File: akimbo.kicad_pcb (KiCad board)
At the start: 2 copper layers, 163.9 x 125.9 mm, 77 parts, among them J1 USB-C, J2 3.5mm TRRS, J3 3.5mm TRRS, K1 -, K11 -, K12 -, K13 -, K14 -, K15 -, K16 -, K17 -, K18 -, K19 -, K2 -, K20 -, K21 -, K22 -, K23 -, K24 -, K25 -, K26 -, K27 -, K28 -, K29 -, K3 -, K30 -, K4 -, K6 -, K7 -, K8 -, K9 -, U1 ATmega32U4, U2 MCP23017_SO, Y1 16M

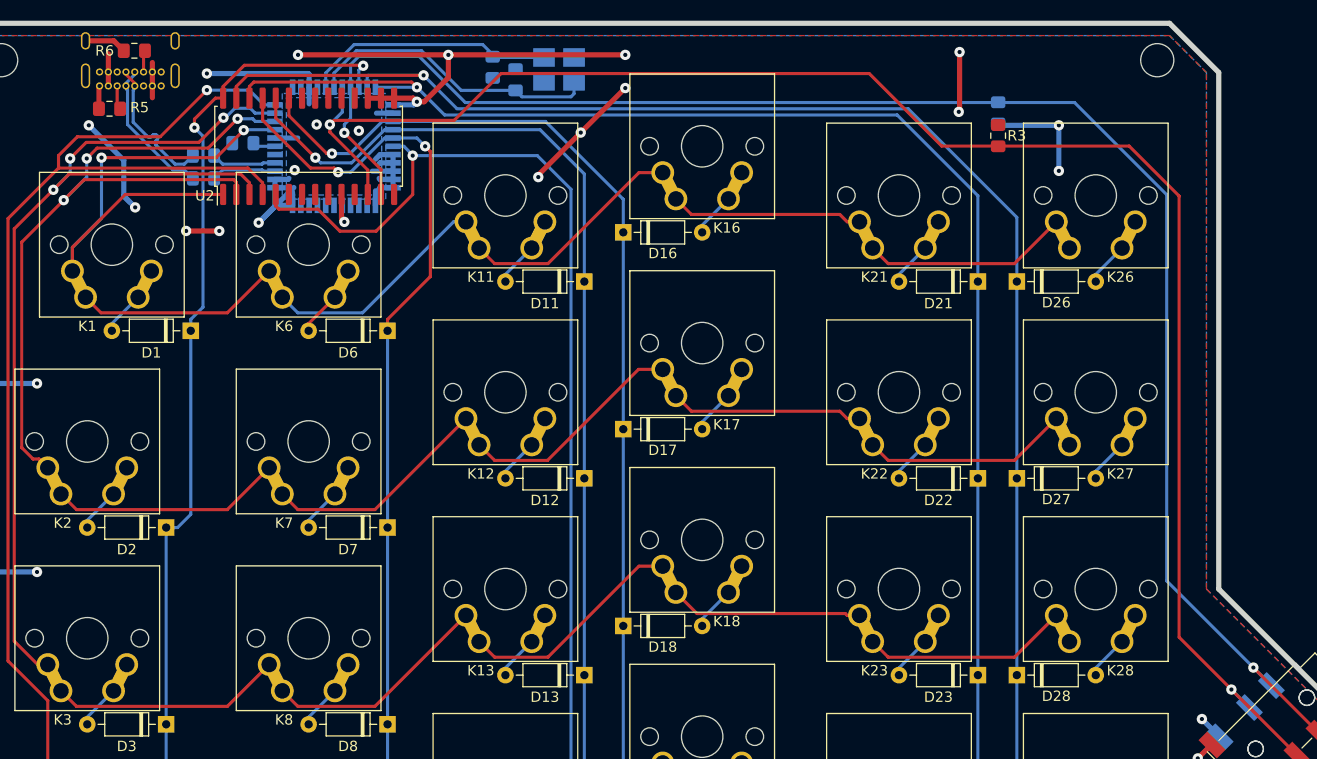
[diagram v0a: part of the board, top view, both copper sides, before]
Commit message: I2C routing improvements
avoids running sda/sck too close to the crystal oscillator
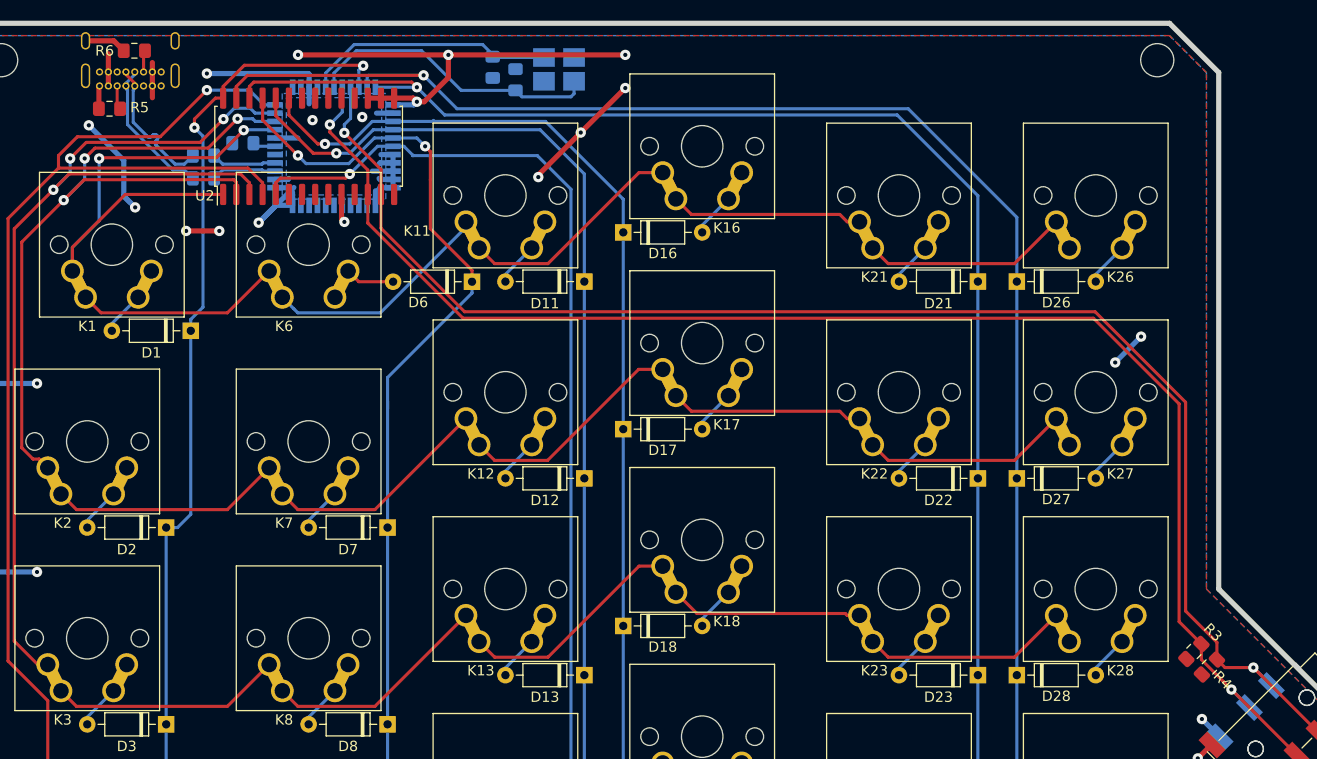
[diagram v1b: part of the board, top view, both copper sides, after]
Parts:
- R4: moved to F.Cu
- moved R4 57.3 mm to (141.6, 85.9), turned to 45 degrees
- moved R3 53.3 mm to (140.1, 84.4), turned to 45 degrees
- moved D6 9.43 mm to (70.4, 48.7)
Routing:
- net /sck: track 162.5 -> 141.8 mm
- net /sda: track 159.5 -> 141.3 mm
- net +5V: track 88.6 -> 81.1 mm, vias 16 -> 15
- net /row4: track 218.8 -> 212.2 mm
- net GND: track 87.2 -> 81.4 mm, vias 15 -> 13
- net /col1: track 98.3 -> 101.7 mm
- net /col2: track 189.3 -> 188.4 mm
- net /col3: track 189.1 -> 188.3 mm

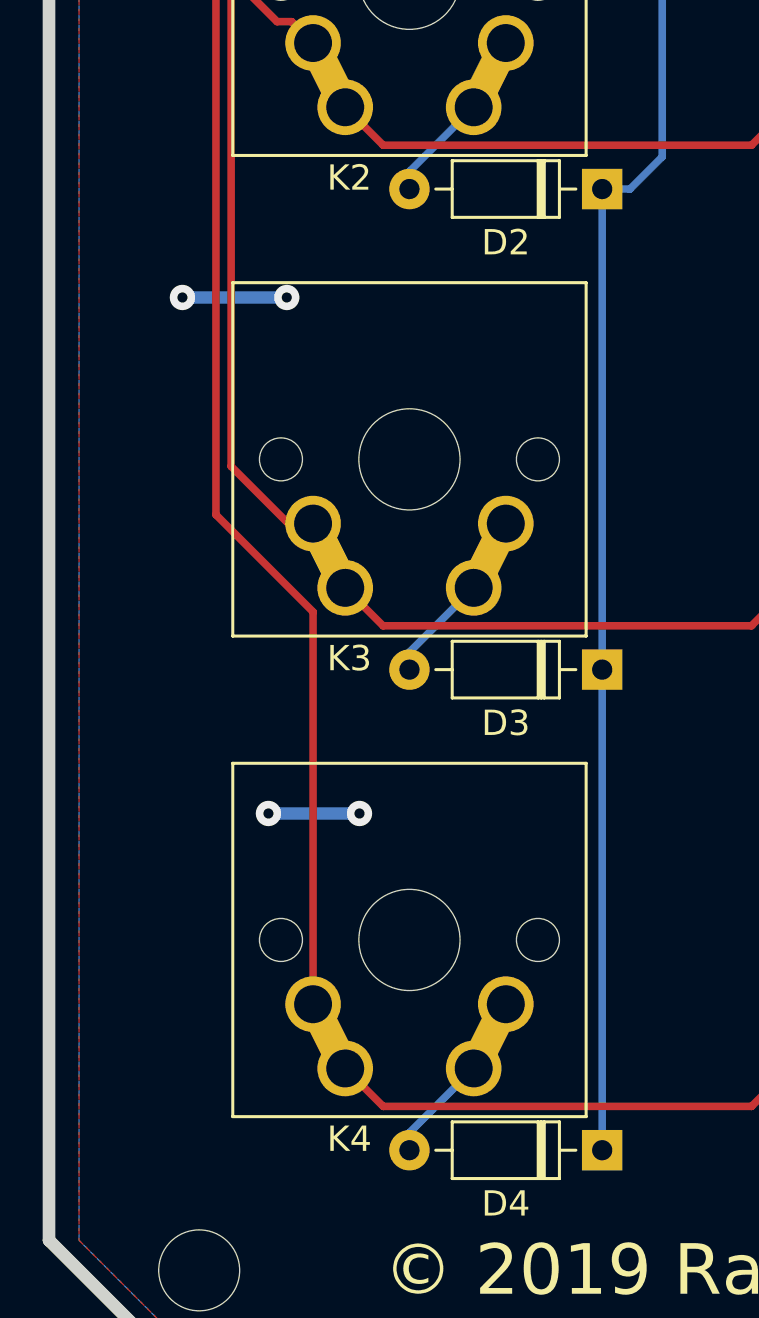
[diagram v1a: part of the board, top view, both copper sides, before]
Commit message: schematic cleanup, BOM essentially complete
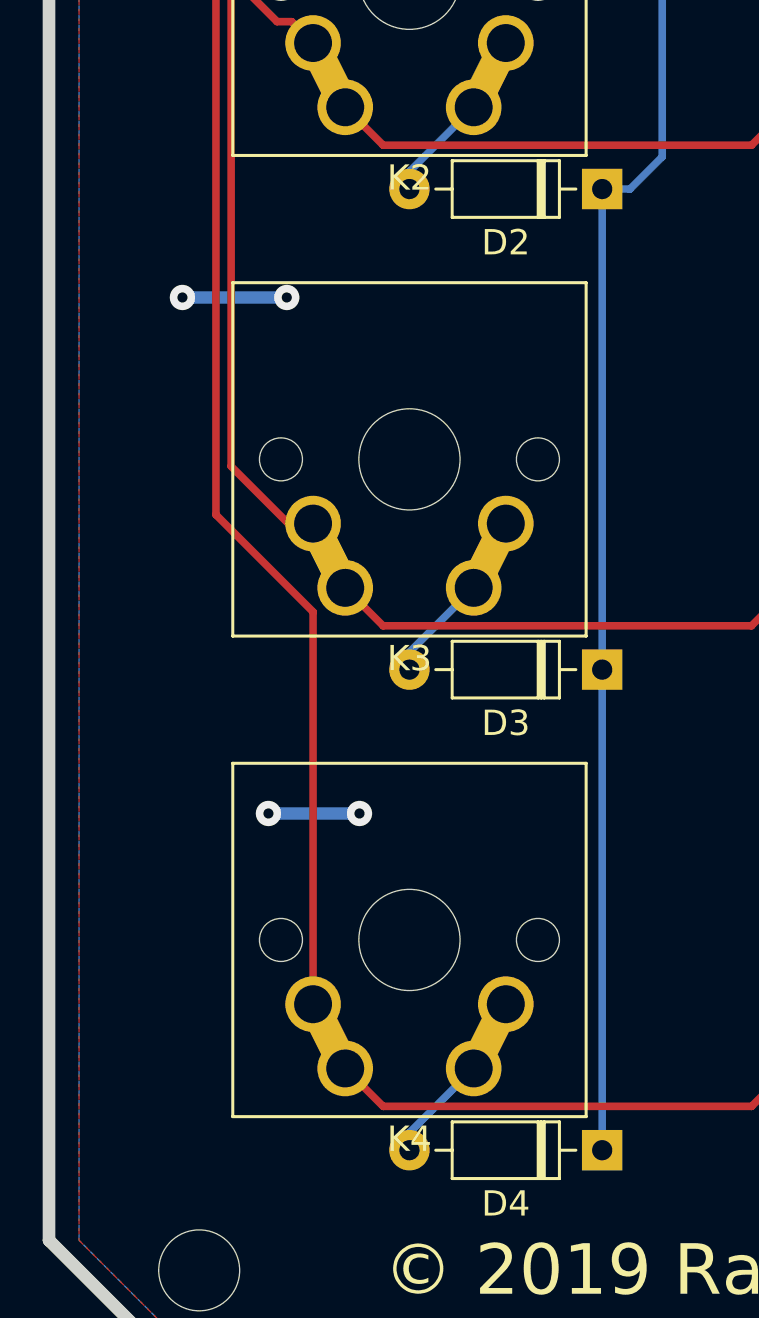
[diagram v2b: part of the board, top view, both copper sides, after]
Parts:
- K2, K3, K4: footprint akimbo:SW_Cherry_MX_1.25u_PCB_Reversible -> akimbo:SW_Cherry_MX_1.00u_PCB_Reversible

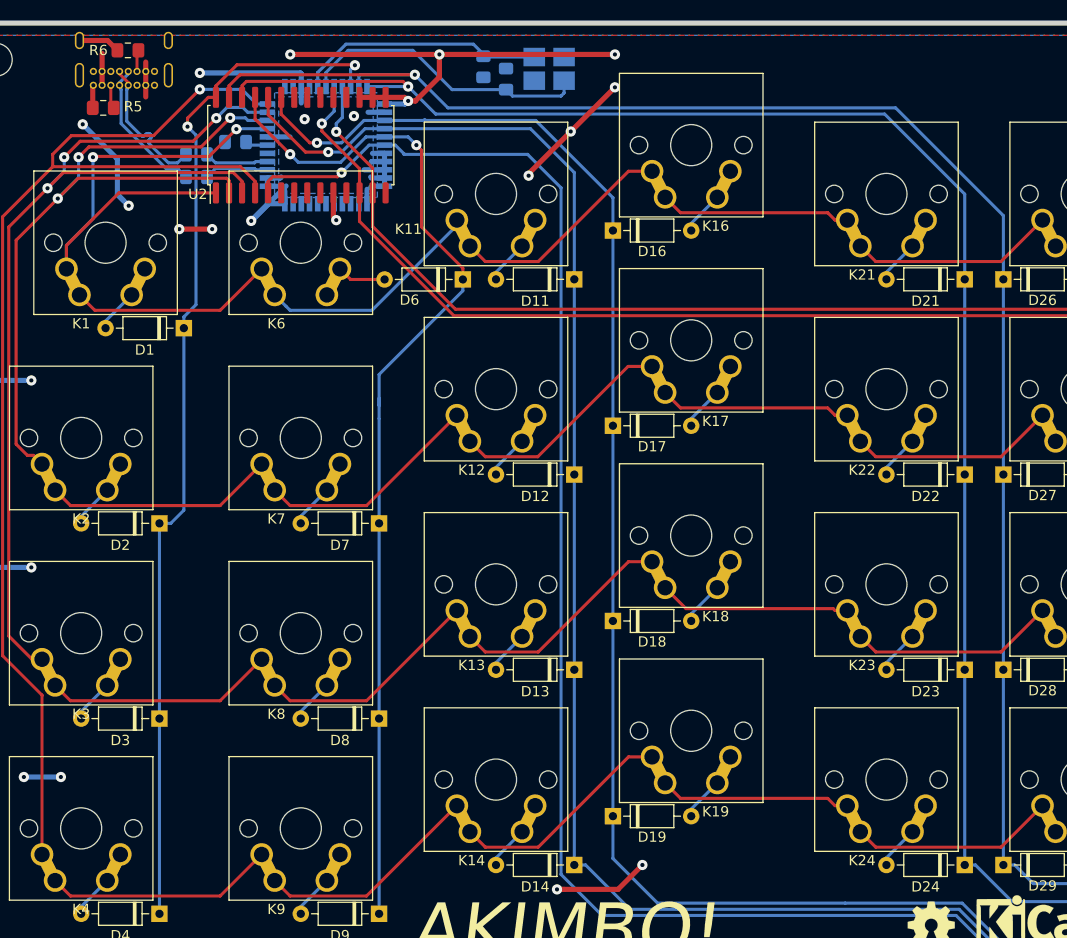
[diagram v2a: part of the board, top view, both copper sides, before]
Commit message: decoupling caps; better crystal-μC routing
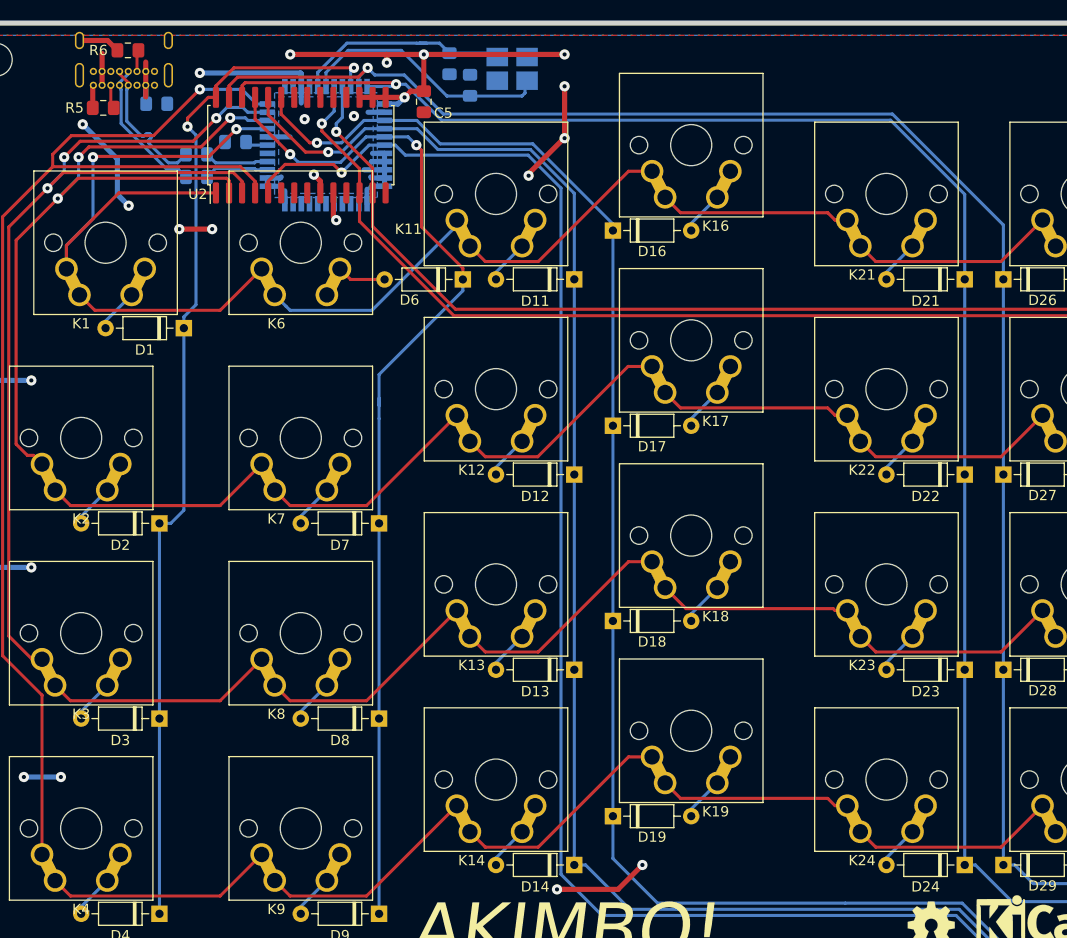
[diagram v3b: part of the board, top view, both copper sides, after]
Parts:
- added C4: 10u, Capacitor_SMD:C_0805_2012Metric_Pad1.15x1.40mm_HandSolder, B.Cu at (40.6, 31.6)
- added C5: 10n, Capacitor_SMD:C_0805_2012Metric_Pad1.15x1.40mm_HandSolder, F.Cu at (66.6, 31.4)
- moved Y1 3.60 mm to (75.2, 28.2)
- moved C3 3.55 mm to (71.1, 29.8)
- moved C2 3.31 mm to (69.1, 27.7)
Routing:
- net +5V: track 81.1 -> 72.1 mm
- net GND: track 81.4 -> 74.2 mm, vias 13 -> 14
- net /col5: track 173.7 -> 169.3 mm
- net Net-(C3-Pad1): track 28.6 -> 24.8 mm
- net Net-(C2-Pad1): track 24.1 -> 21.3 mm
- net /col3: track 188.3 -> 186.6 mm
- net /col4: track 169.6 -> 168.4 mm
- net /col2: track 188.4 -> 187.3 mm
- net /row4: track 212.2 -> 212.8 mm
- net /col0: track 101.3 -> 100.7 mm

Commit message: minor tweaks, no functional changes
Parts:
- REF**: value OSHW-Logo2_7.3x6mm_SilkScreen -> OSHW-Logo_5.7x6mm_SilkScreen; footprint Symbol:OSHW-Logo2_7.3x6mm_SilkScreen -> Symbol:OSHW-Logo_5.7x6mm_SilkScreen
- moved H4 3.36 mm to (168.6, 135.4)
- moved H1 2.38 mm to (24.9, 29.7)
- moved H2 2.38 mm to (24.9, 112.8)
- moved H3 2.38 mm to (136.6, 29.7)
- moved REF** 0.76 mm to (126.7, 112.4)
- moved REF** 0.52 mm to (116.0, 112.5)
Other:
- outline, holes or cut-outs redrawn
- board text added: "Released subject to the terms of the CERN Open Hardware License, v1.2 See LICENSE in the git repository for details"
